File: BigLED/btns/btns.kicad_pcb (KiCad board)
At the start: 2 copper layers, 21 parts, among them J1 MainBrd, J2 Prog, J3 DBG, SW1 TSX101G100-250, SW2 RotaryEncoder_Switch, SW3 SW_Push, SW4 SW_Push, SW5 SW_Push, SW6 SW_Push, SW7 SW_Push, SW8 SW_Push, SW9 SW_Push, U1 PY32F002AF15P6TU, U3 74LVC2G66, U4 SSD1306 OLED

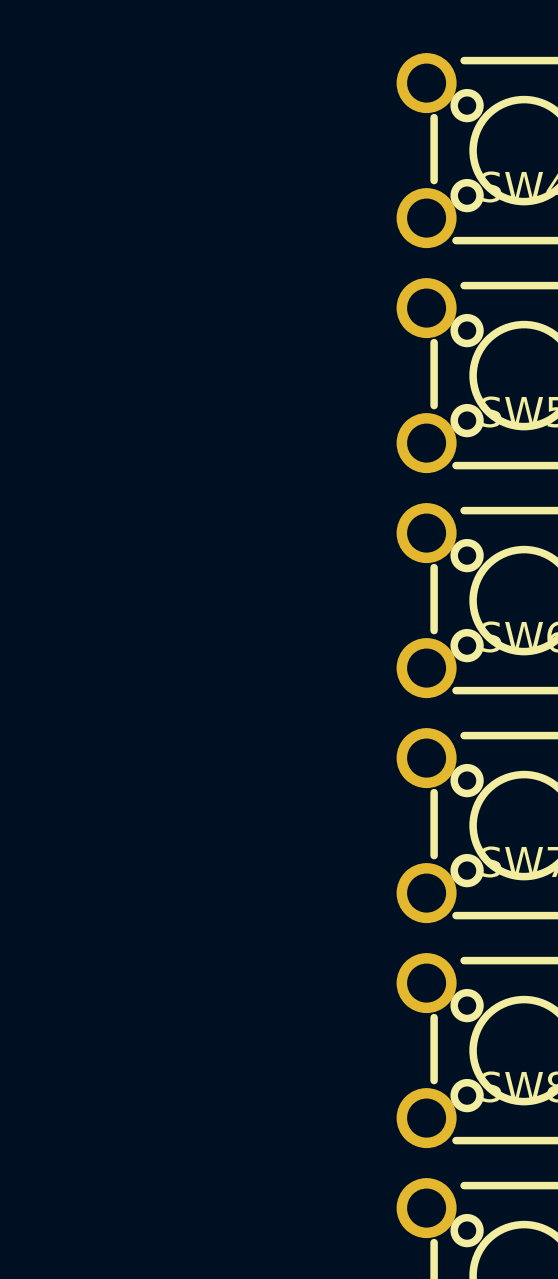
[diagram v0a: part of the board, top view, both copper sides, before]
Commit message: PCB for BigLED Panel started
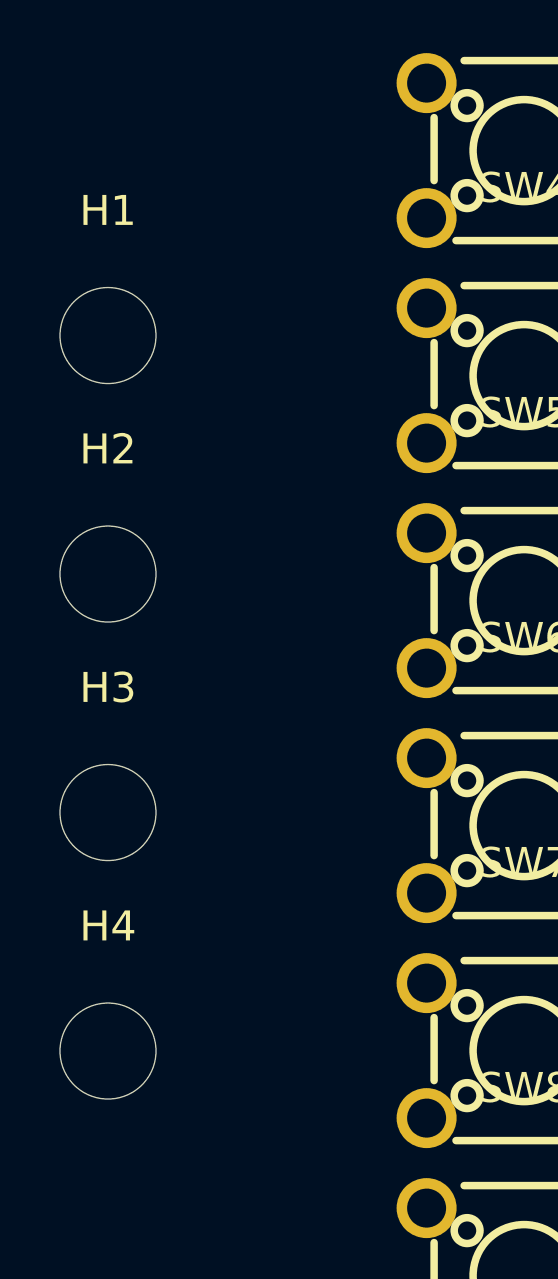
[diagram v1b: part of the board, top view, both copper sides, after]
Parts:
- added H1: MountingHole, MountingHole:MountingHole_3.2mm_M3, F.Cu at (89.5, 60.0)
- added H2: MountingHole, MountingHole:MountingHole_3.2mm_M3, F.Cu at (89.5, 67.9)
- added H3: MountingHole, MountingHole:MountingHole_3.2mm_M3, F.Cu at (89.5, 75.9)
- added H4: MountingHole, MountingHole:MountingHole_3.2mm_M3, F.Cu at (89.5, 83.8)

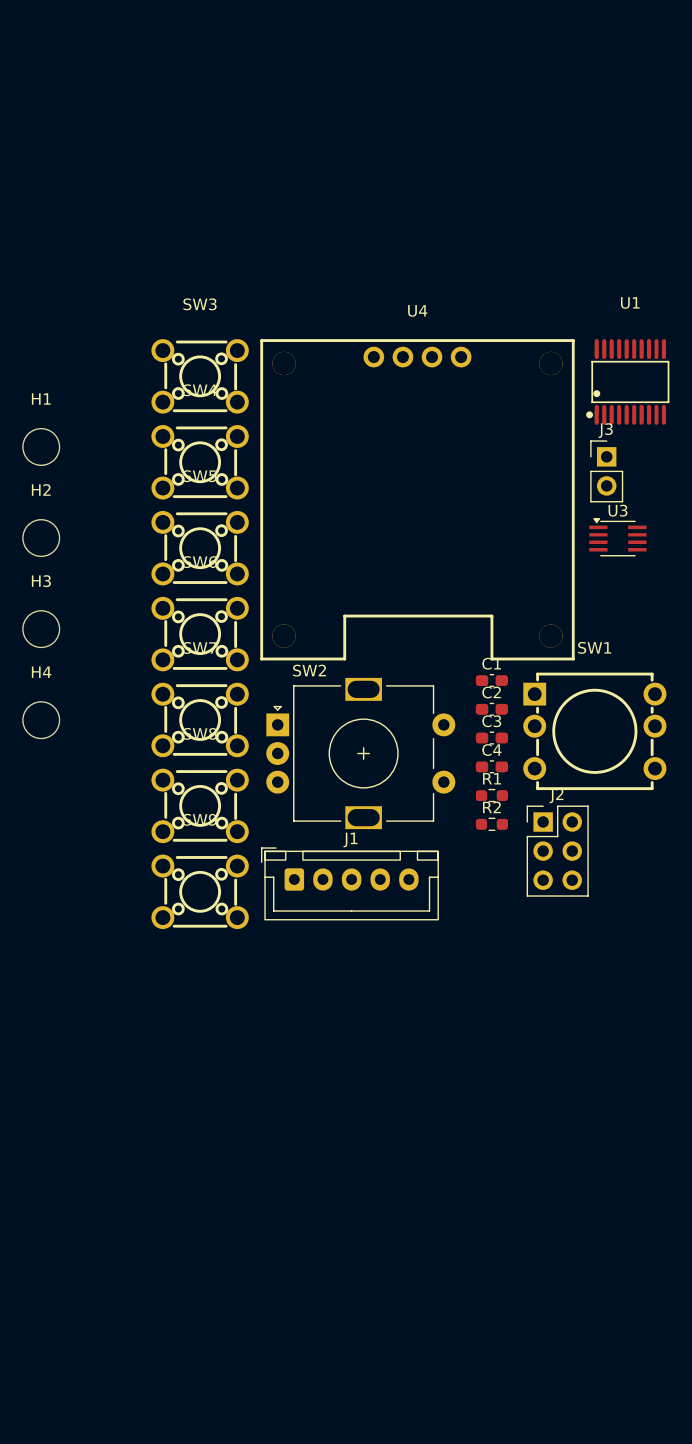
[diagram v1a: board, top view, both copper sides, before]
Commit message: PCB for BigLED Buttons finished
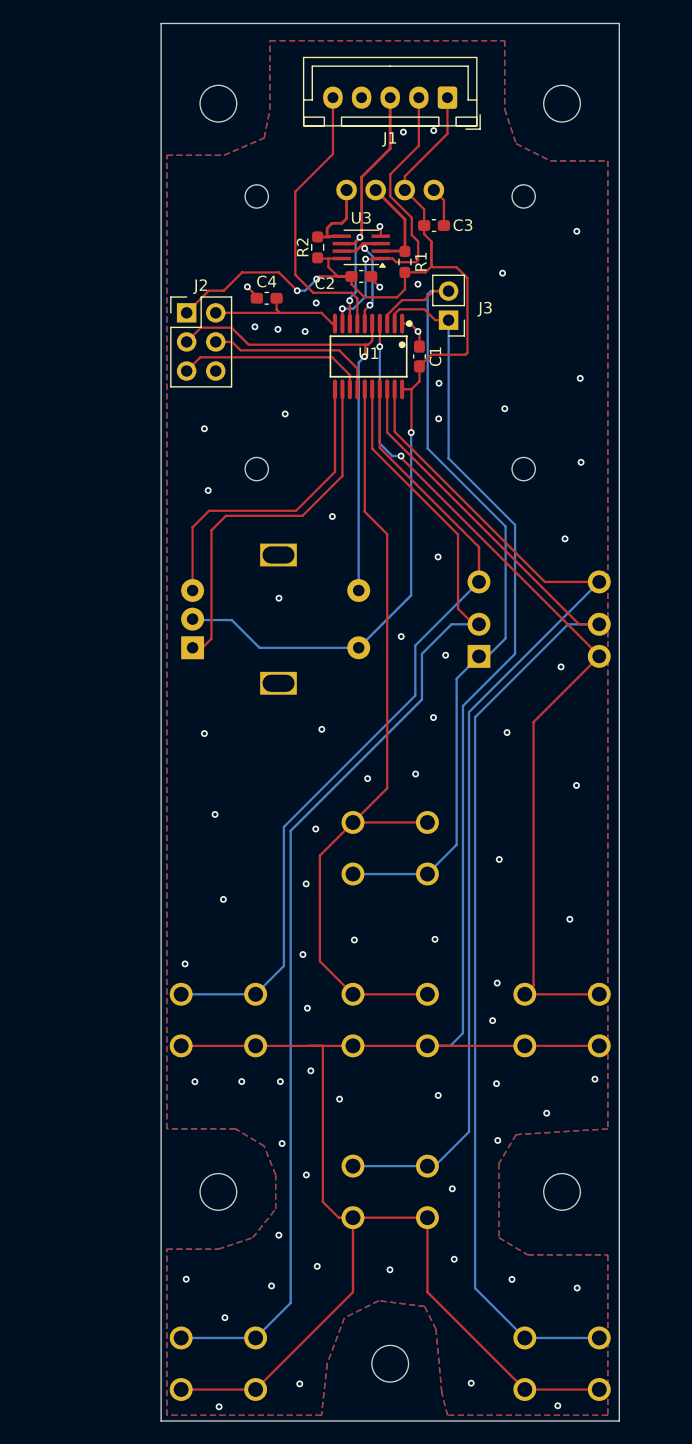
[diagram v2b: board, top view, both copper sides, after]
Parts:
- added H5: MountingHole, MountingHole:MountingHole_3.2mm_M3, F.Cu at (120.0, 140.0)
- SW1, SW2, SW3, SW4, SW5, SW6, SW7, SW8, SW9, U4: moved to B.Cu
- moved SW5 77.9 mm to (135.0, 140.0)
- moved J1 69.6 mm to (125.0, 29.5), turned to 180 degrees
- moved H3 66.9 mm to (135.0, 125.0)
- moved H2 59.2 mm to (135.0, 30.0)
- moved SW4 58.0 mm to (135.0, 110.0)
- moved SW3 56.2 mm to (105.0, 110.0)
- moved SW7 56.2 mm to (105.0, 140.0)
- moved J2 54.3 mm to (102.2, 48.3)
- moved R2 52.6 mm to (113.7, 42.5), turned to -90 degrees
- moved SW6 51.4 mm to (120.0, 125.0)
- moved R1 47.2 mm to (121.3, 43.8), turned to -90 degrees
- moved C4 45.4 mm to (109.2, 47.0)
- moved C3 45.0 mm to (123.8, 40.6)
- moved H4 44.0 mm to (105.0, 125.0)
- moved C2 39.5 mm to (117.5, 45.1), turned to 180 degrees
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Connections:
- C4 pad 2: Net-(J2-Pin_3) -> Net-(J2-Pin_2)
- SW2 pad A: Net-(U1-PA6) -> /QE-A
- SW2 pad B: Net-(U1-PB3) -> /QE-B
- SW2 pad S1: Net-(J2-Pin_2) -> Net-(J2-Pin_3)
- U1 pad 10: Net-(J2-Pin_3) -> Net-(J2-Pin_2)
- U1 pad 11: /B6 -> /QE-B
- U1 pad 12: /B5 -> /QE-A
- U1 pad 13: Net-(J2-Pin_4) -> Net-(J2-Pin_5)
- U1 pad 14: Net-(J2-Pin_5) -> Net-(J2-Pin_4)
- U1 pad 15: /B4 -> /B6
- U1 pad 16: /B3 -> /B5
- U1 pad 17: /B2 -> /B4
- U1 pad 18: /B1 -> /B2
- U1 pad 19: Net-(U1-PB1) -> /B3
- U1 pad 4: Net-(U1-PB3) -> /B1
- U1 pad 5: Net-(J2-Pin_2) -> Net-(J2-Pin_3)
- U1 pad 6: Net-(U1-PA6) -> /Enable
- U3 pad 3: Net-(U1-PB1) -> /Enable
- U3 pad 5: /SDA -> Net-(U4-SDA)
- U3 pad 6: Net-(U4-SDA) -> /SDA
- U3 pad 7: Net-(U1-PB1) -> /Enable
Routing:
- net Net-(J3-Pin_1): track 0.00 -> 187.2 mm
- net +3.3V: track 0.00 -> 109.6 mm, vias 0 -> 3
- net /B2: track 0.00 -> 105.9 mm
- net /B5: track 0.00 -> 102.9 mm
- net /B3: track 0.00 -> 91.1 mm
- net /B1: track 0.00 -> 77.1 mm, vias 0 -> 2
- net Net-(J3-Pin_2): track 0.00 -> 72.1 mm
- net /B4: track 0.00 -> 71.0 mm
- net /B6: track 0.00 -> 70.3 mm
- net Net-(J2-Pin_3): track 0.00 -> 40.7 mm, vias 0 -> 1
- net /QE-A: track 0.00 -> 32.4 mm
- net /SCL: track 0.00 -> 28.1 mm, vias 0 -> 2
- net /QE-B: track 0.00 -> 27.2 mm
- net /INT: track 0.00 -> 25.3 mm
- net /SDA: track 0.00 -> 23.0 mm, vias 0 -> 2
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- added copper zone on B.Cu, net GND
- added copper zone on F.Cu, net GND
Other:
- board outline added: 40 x 122 mm
